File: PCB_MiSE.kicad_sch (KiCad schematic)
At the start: 35 parts, among them IC1 MSP430FR2355TPT, J1 WIFI, J2 Conn_01x03, J4 Clk read conn, J6 Display, J7 I2C read, J8 Conn_02x07_Odd_Even, SW1 SW_Push, SW2 SW_Push, SW3 SW_Push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

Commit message: modifico footprints LDRs
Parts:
- R15, R8: footprint OptoDevice:R_LDR_10x8.5mm_P7.6mm_Vertical -> Connector_PinHeader_2.54mm:PinHeader_1x02_P2.54mm_Horizontal
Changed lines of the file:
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@@
 			)
 		)
-		(property "Footprint" "OptoDevice:R_LDR_10x8.5mm_P7.6mm_Vertical"
+		(property "Footprint" "Connector_PinHeader_2.54mm:PinHeader_1x02_P2.54mm_Horizontal"
 			(at 55.245 119.38 90)
 			(effects
@@
 			)
 		)
-		(property "Footprint" "OptoDevice:R_LDR_10x8.5mm_P7.6mm_Vertical"
+		(property "Footprint" "Connector_PinHeader_2.54mm:PinHeader_1x02_P2.54mm_Horizontal"
 			(at 503.555 93.98 90)
 			(effects

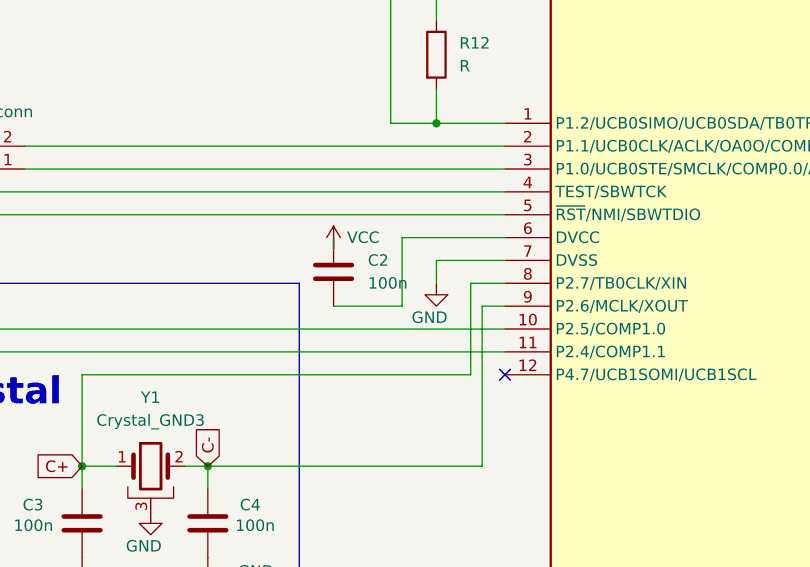
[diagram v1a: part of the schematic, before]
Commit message: Falta agregar net classes y corregir los errores de diseño
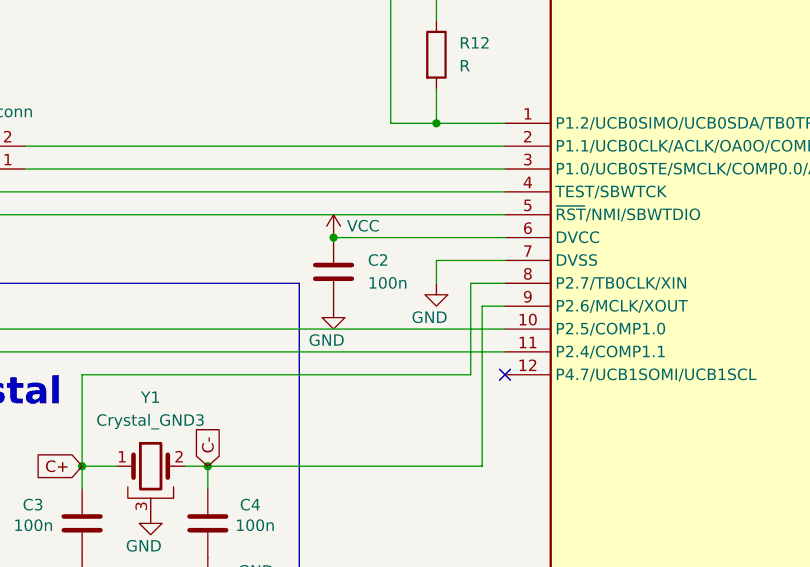
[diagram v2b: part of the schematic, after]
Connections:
- net GND: now also C2.2
- net VCC: now also IC1.6 (DVCC)
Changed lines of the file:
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@@
 	)
 	(junction
+		(at 227.33 205.74)
+		(diameter 0)
+		(color 0 0 0 0)
+	)
+	(junction
 		(at 97.79 335.28)
 		(diameter 0)
@@
 	(wire
 		(pts
-			(xy 234.95 205.74) (xy 246.38 205.74)
+			(xy 227.33 205.74) (xy 246.38 205.74)
 		)
 		(stroke
@@
 	(wire
 		(pts
-			(xy 227.33 213.36) (xy 234.95 213.36)
-		)
-		(stroke
-			(width 0)
-			(type default)
-		)
-	)
-	(wire
-		(pts
 			(xy 36.83 212.09) (xy 43.18 212.09)
 		)
@@
 	(wire
 		(pts
-			(xy 227.33 207.01) (xy 227.33 205.74)
-		)
-		(stroke
-			(width 0)
-			(type default)
-		)
-	)
-	(wire
-		(pts
 			(xy 556.26 219.71) (xy 558.8 219.71)
 		)
@@
 	(wire
 		(pts
-			(xy 234.95 205.74) (xy 234.95 213.36)
-		)
-		(stroke
-			(width 0)
-			(type default)
-		)
-	)
-	(wire
-		(pts
 			(xy 481.33 99.06) (xy 499.11 99.06)
 		)
@@
 	(symbol
 		(lib_id "power:VCC")
-		(at 227.33 207.01 0)
+		(at 227.33 205.74 0)
 		(unit 1)
 		(exclude_from_sim no)
@@
 		(dnp no)
 		(property "Reference" "#PWR010"
-			(at 227.33 210.82 0)
+			(at 227.33 209.55 0)
 			(effects
 				(font
@@
 		)
 		(property "Value" "VCC"
-			(at 230.632 205.74 0)
+			(at 230.632 204.47 0)
 			(effects
 				(font
@@
 		)
 		(property "Footprint" ""
-			(at 227.33 207.01 0)
+			(at 227.33 205.74 0)
 			(effects
 				(font
@@
 		)
 		(property "Datasheet" ""
-			(at 227.33 207.01 0)
+			(at 227.33 205.74 0)
 			(effects
 				(font
@@
 		)
 		(property "Description" "Power symbol creates a global label with name \"VCC\""
-			(at 227.33 207.01 0)
+			(at 227.33 205.74 0)
 			(effects
 				(font
@@
 		(on_board yes)
 		(dnp no)
-		(fields_autoplaced yes)
 		(property "Reference" "C2"
 			(at 231.14 208.2799 0)
@@
 					(unit 1)
 				)
+			)
+		)
+	)
+	(symbol
+		(lib_id "power:GND")
+		(at 227.33 213.36 0)
+		(unit 1)
+		(exclude_from_sim no)
+		(in_bom yes)
+		(on_board yes)
+		(dnp no)
+		(property "Reference" "#PWR024"
+			(at 227.33 219.71 0)
+			(effects
+				(font
+					(size 1.27 1.27)
+				)
+				(hide yes)
+			)
+		)
+		(property "Value" "GND"
+			(at 226.568 217.17 0)
+			(effects
+				(font
+					(size 1.27 1.27)
+				)
+			)
+		)
+		(property "Footprint" ""
+			(at 227.33 213.36 0)
+			(effects
+				(font
+					(size 1.27 1.27)
+				)
+				(hide yes)
+			)
+		)
+		(property "Datasheet" ""
+			(at 227.33 213.36 0)
+			(effects
+				(font
+					(size 1.27 1.27)
+				)
+				(hide yes)
+			)
+		)
+		(property "Description" "Power symbol creates a global label with name \"GND\" , ground"
+			(at 227.33 213.36 0)
+			(effects
+				(font
+					(size 1.27 1.27)
+				)
+				(hide yes)
+			)
+		)
+		(pin "1"
+		)
+		(instances
+			(project "PCB_MiSE"
+				(path "/d767662d-a2fb-4431-89c7-c67b7c23601b"
+					(reference "#PWR024")
+					(unit 1)
+				)
